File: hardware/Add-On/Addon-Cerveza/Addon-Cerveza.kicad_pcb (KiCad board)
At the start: 2 copper layers, 41.2 x 49.5 mm, 23 parts, among them J1 Conn_02x03_Odd_Even, SW2 On, SW7 RESET, U1 TMP102xxDRL, U2 CH32V003F4U6

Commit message: feat(Hw):Init_Route_Add_On_Cerveza
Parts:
- added ?: , , F.Cu at (88.4, 49.0)
- moved C8 5.69 mm to (82.9, 54.3)
- moved SW7 5.28 mm to (79.2, 54.3), turned to -90 degrees
- moved C7 2.50 mm to (92.4, 54.1)
- moved U2 2.50 mm to (90.1, 60.4)
- moved G*** 0.63 mm to (90.5, 70.0)
- moved C1 0.51 mm to (95.2, 78.7)
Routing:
- net +3V3: track 0.00 -> 124.1 mm, vias 0 -> 3
- net /NEOPIXELES: track 0.00 -> 39.0 mm
- net Net-(BT1--): track 0.00 -> 35.9 mm, vias 0 -> 4
- net /ALERT: track 0.00 -> 33.0 mm, vias 0 -> 3
- net /SWDIO: track 0.00 -> 31.4 mm, vias 0 -> 2
- net /SWCLK: track 0.00 -> 25.4 mm, vias 0 -> 2
- net /SCL: track 0.00 -> 20.3 mm, vias 0 -> 1
- net /SDA: track 0.00 -> 18.0 mm, vias 0 -> 1
- net /RST: track 0.00 -> 17.4 mm
- net GND: track 0.00 -> 12.7 mm, vias 0 -> 8
- net Net-(D11-DIN): track 0.00 -> 2.67 mm

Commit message: feat(Hw):Update_Schematic_And_Route_Addon_Cerveza
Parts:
- added JP1: Jumper, Jumper:SolderJumper-2_P1.3mm_Bridged_RoundedPad1.0x1.5mm, B.Cu at (92.9, 82.9)
- added R4: 10k, Resistor_SMD:R_0603_1608Metric, B.Cu at (95.3, 82.5)
- R1, R2: value 5K -> 4.7K
- R3: value 5K -> 10k
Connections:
- U1 pad 4: GND -> Net-(U1-ADD0)
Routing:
- net Net-(U1-ADD0): track 0.00 -> 2.54 mm, vias 0 -> 1
- net +3V3: track 124.1 -> 126.3 mm
- net Net-(JP1-B): track 0.00 -> 1.91 mm
- net GND: track 12.7 -> 12.1 mm, vias 8 -> 7

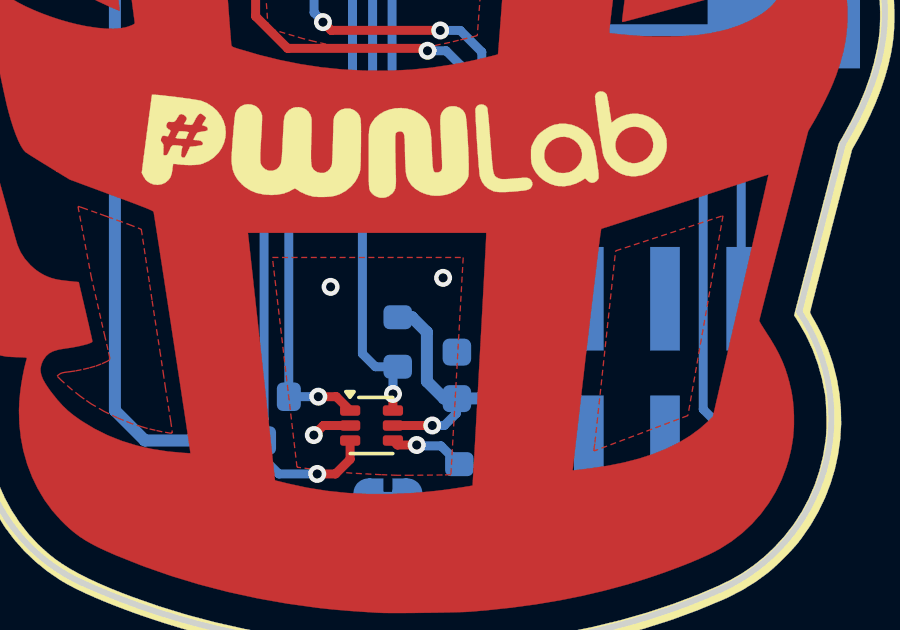
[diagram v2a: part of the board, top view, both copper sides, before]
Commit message: feat(Hw):Update_Labels
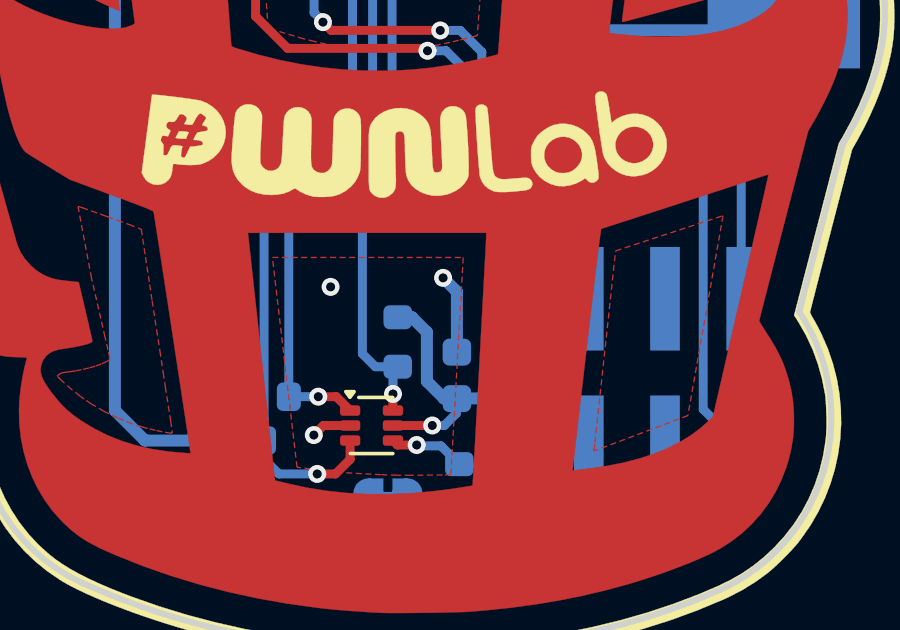
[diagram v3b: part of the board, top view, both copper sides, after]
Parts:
- moved G*** 1.66 mm to (90.5, 71.6)
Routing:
- net GND: track 12.1 -> 14.7 mm
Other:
- board text added: "SPONSORED BY"
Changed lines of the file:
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@@
 	(footprint "Aesthetics:electronic_cats_logo_8x6"
 		(layer "B.Cu")
-		(at 90.46 69.97 180)
+		(at 90.45 71.63 180)
 		(property "Reference" "G***"
 			(at 0 0 0)
@@
 		(layer "Edge.Cuts")
 	)
+	(gr_text "SPONSORED BY"
+		(at 90.46 66.95 0)
+		(layer "B.SilkS")
+		(effects
+			(font
+				(size 1 1)
+				(thickness 0.2)
+				(bold yes)
+			)
+			(justify mirror)
+		)
+	)
 	(segment
 		(start 94.378732 80.351268)
@@
 	)
 	(segment
+		(start 95.2 75.89)
+		(end 94.74 75.43)
+		(width 0.4)
+		(layer "B.Cu")
+		(net 3)
+	)
+	(segment
 		(start 91.09 57.545)
 		(end 91.09 58.78)
@@
 		(width 0.4)
 		(layer "B.Cu")
+		(net 3)
+	)
+	(segment
+		(start 95.2 77.905)
+		(end 95.2 75.89)
+		(width 0.4)
+		(layer "B.Cu")
